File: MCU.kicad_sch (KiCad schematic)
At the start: 21 parts

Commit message: MCU updated to 48 pin
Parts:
- removed C58, C59, C71 (x2), C72, C73, C78 (x2): 0.1uF, Power_Analyzer:C_0603_1608Metric, symbol Power_Analyzer:0.1uF
- removed C74: 10uF, Power_Analyzer:C_0805_2012Metric, symbol Power_Analyzer:10uF
- removed C83: 2.2uF, Power_Analyzer:C_0603_1608Metric, symbol Power_Analyzer:2.2uF
- removed C?: 0.1uF, Capacitor_SMD:C_0603_1608Metric, symbol Major_Project:0.1uF
- removed C? (x2): 2.2uF, Capacitor_SMD:C_0603_1608Metric, symbol Major_Project:2.2uF
- removed R? (x2): 4.7K, Resistor_SMD:R_1206_3216Metric, symbol Major_Project:4.7K
- removed R? (x2): 10K, Resistor_SMD:R_1206_3216Metric, symbol Major_Project:10K
- removed U? (x4): F280037CSPZ, LQFP100_PZ_TEX, symbol Major_Project:F280037CSPZ
- added C1, C7: 2.2uF, Capacitor_SMD:C_0603_1608Metric, symbol Major_Project:2.2uF
- added C10, C2, C4, C5, C6, C8, C9: 0.1uF, Capacitor_SMD:C_0603_1608Metric, symbol Major_Project:0.1uF
- added C3: 10uF, Capacitor_SMD:C_0603_1608Metric, symbol Major_Project:10uF
- added J6: JTAG, Power_Analyzer:SAMTEC_FTSH-105-01-F-DV-K, symbol Power_Analyzer:FTSH-105-01-F-DV-K
- added R1, R4: 4.7K, Resistor_SMD:R_1206_3216Metric, symbol Major_Project:4.7K
- added R2, R3: 10K, Resistor_SMD:R_1206_3216Metric, symbol Major_Project:10K
- added U1: F280037CSPT, Power_Analyzer:PT0048A-MFG, symbol Major_Project:F280037CSPT
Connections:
- net +3.3V_2: now also C1.1, C10.1, C7.1, C8.1, C9.1, J6.01, R1.1, R2.1, R3.1, R4.1, U1.12 (VREFHI), U1.18 (VDDA), U1.24 (VDDIO), U1.35 (VDDIO), U1.46 (VDDIO)
- net GND_2: now also C1.2, C10.2, C2.2, C3.2, C4.2, C5.2, C6.2, C7.2, C8.2, C9.2, J6.03, J6.05, J6.09, U1.13 (VREFLO), U1.17 (VSSA), U1.22 (VSS), U1.37 (VSS), U1.44 (VSS)
- new net: C3.1, C4.1, C5.1, C6.1, U1.23 (VDD), U1.36 (VDD), U1.45 (VDD)
- new net: C2.1, R4.2, U1.3 (XRS_N)
- new net TCK: J6.04, U1.28 (TCK)
- new net TDI: J6.08, R2.2, U1.31 (GPIO35_TDI)
- new net TDO: J6.06, R3.2, U1.29 (GPIO37_TDO)
- new net TMS: J6.02, R1.2, U1.30 (TMS)
- no-connect marks 1 -> 2

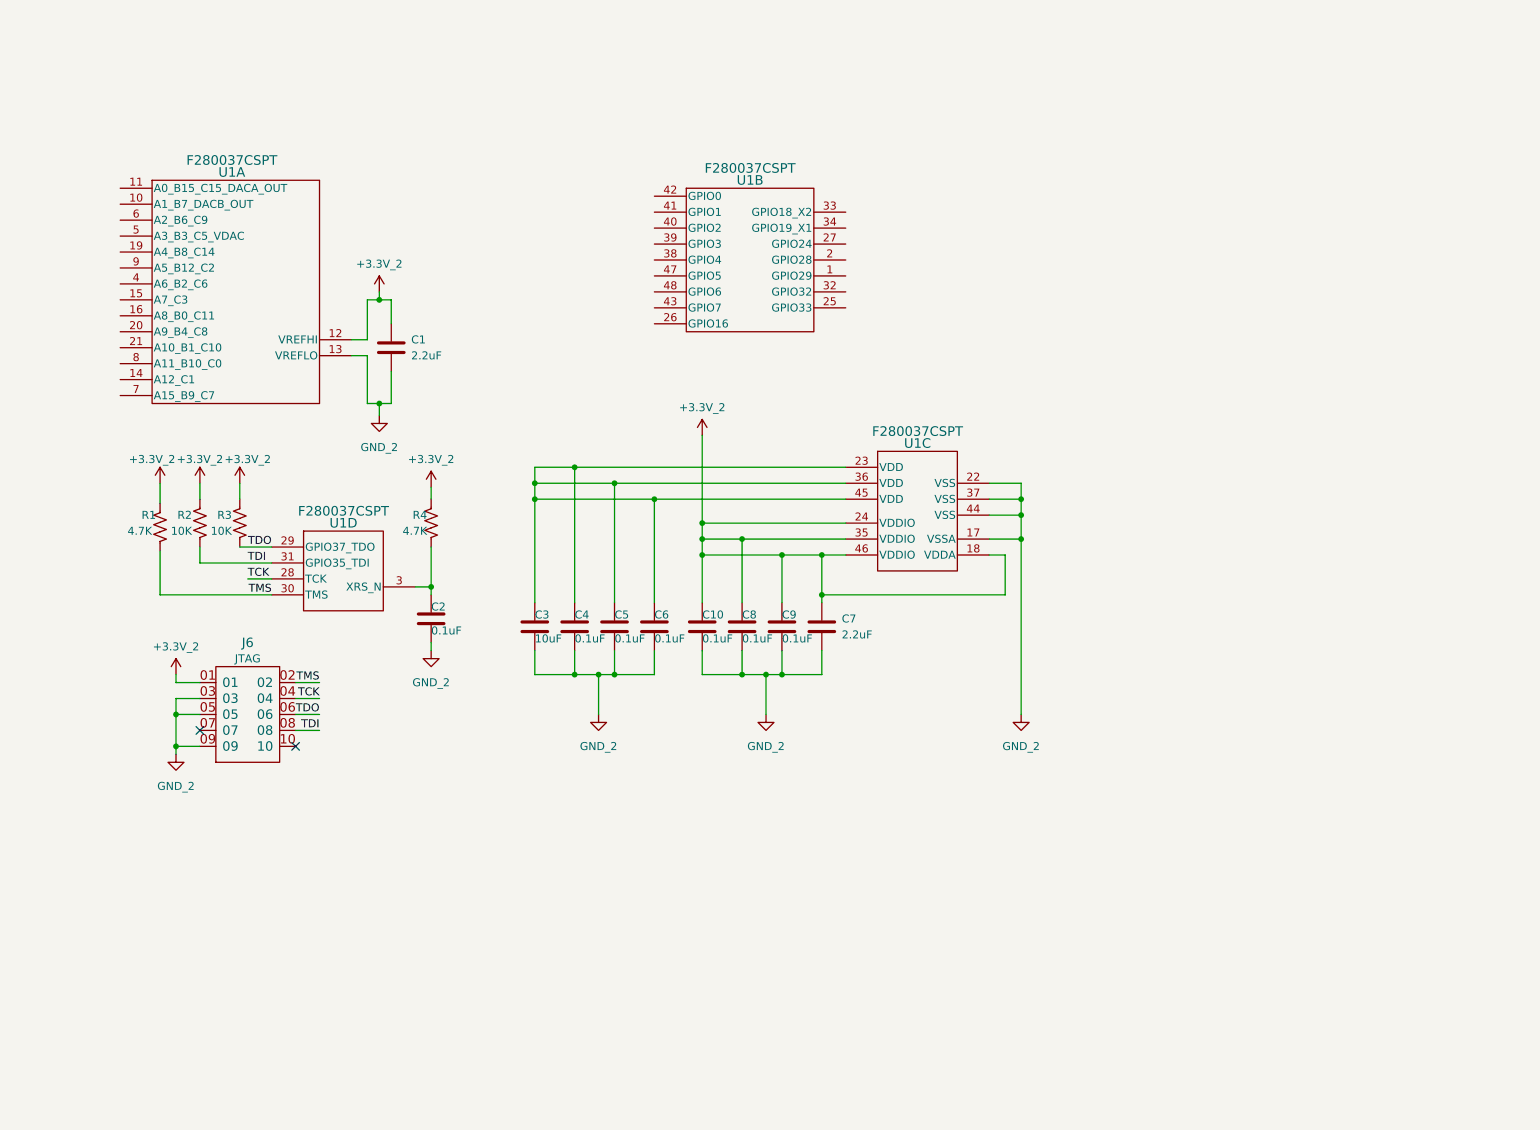
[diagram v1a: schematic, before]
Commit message: Current Sensing added
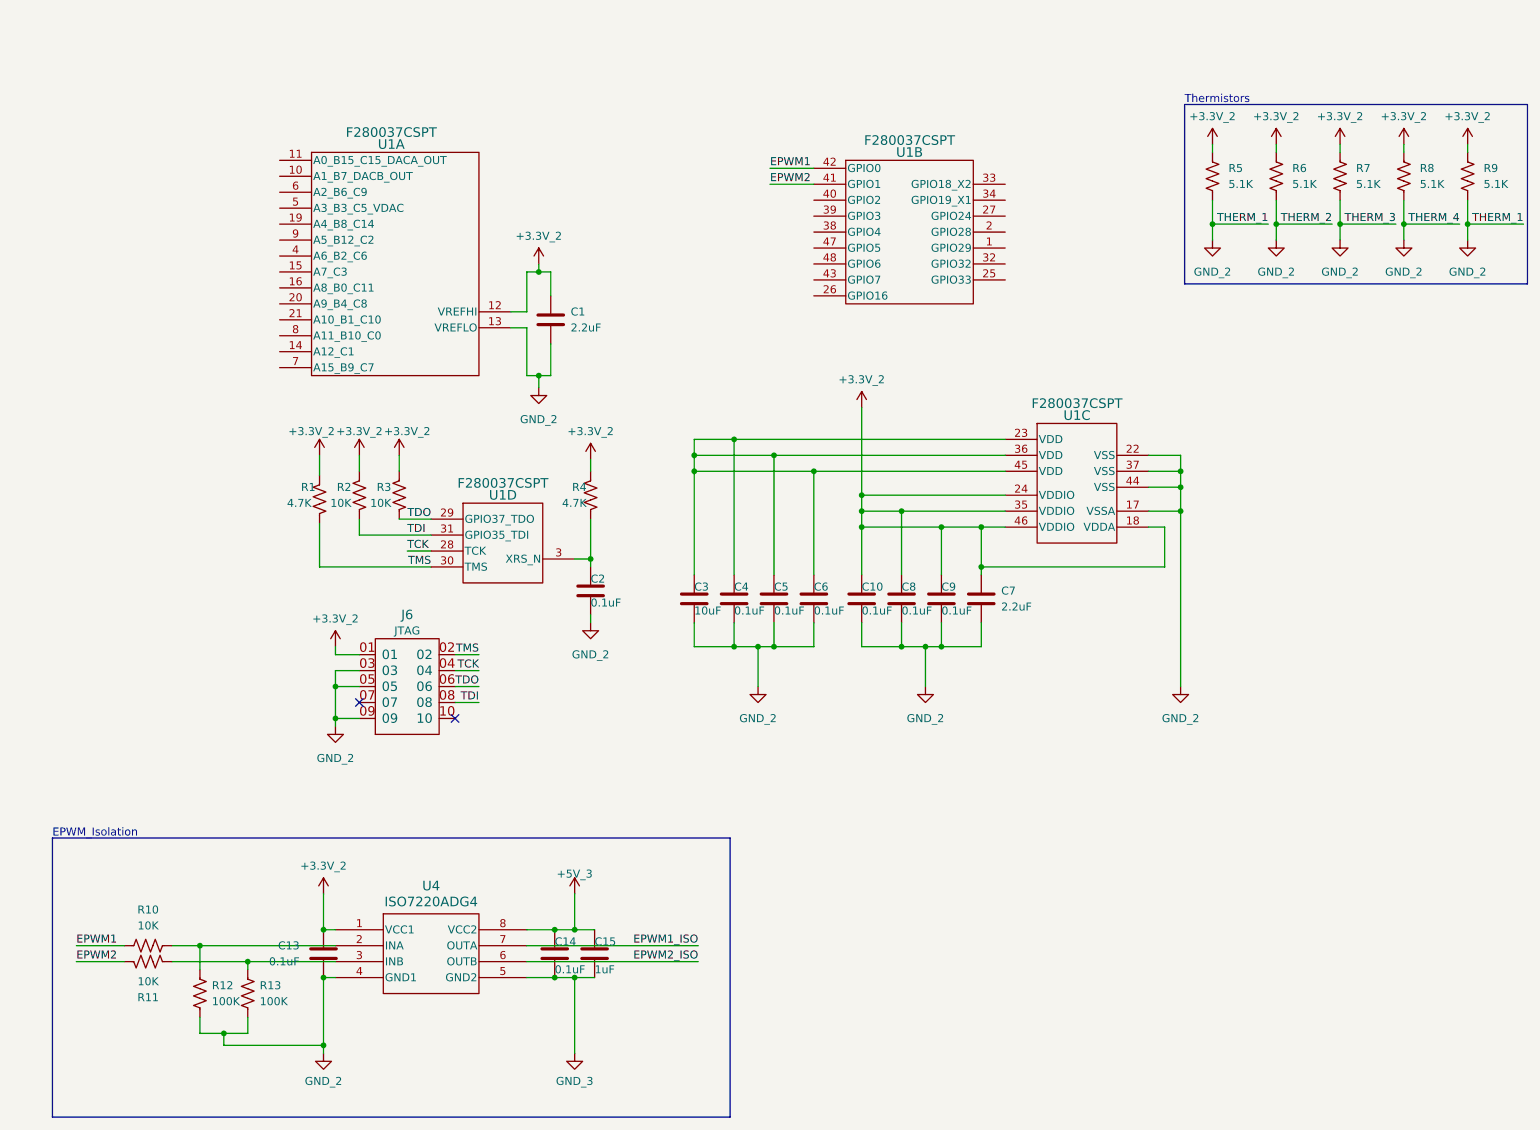
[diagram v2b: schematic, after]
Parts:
- added C13, C14: 0.1uF, Capacitor_SMD:C_0603_1608Metric, symbol Major_Project:0.1uF
- added C15: 1uF, Capacitor_SMD:C_0603_1608Metric, symbol Major_Project:1uF
- added R10, R11: 10K, Resistor_SMD:R_1206_3216Metric, symbol Major_Project:10K
- added R12, R13: 100K, Resistor_SMD:R_1206_3216Metric, symbol Major_Project:100K
- added R5, R6, R7, R8, R9: 5.1K, Resistor_SMD:R_1206_3216Metric, symbol Major_Project:5.1K
- added U4: ISO7220ADG4, D8, symbol Major_Project:ISO7220ADG4
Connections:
- net +3.3V_2: now also C13.1, R5.1, R6.1, R7.1, R8.1, R9.1, U4.1 (VCC1)
- net GND_2: now also C13.2, R12.2, R13.2, R5.2, R6.2, R7.2, R8.2, R9.2, U4.4 (GND1)
- net EPWM2: now reaches U1.41 (GPIO1)
- net EPWM2: now also R11.1
- net EPWM1: now reaches U1.42 (GPIO0)
- net EPWM1: now also R10.1
- new net: R10.2, R12.1, U4.2 (INA)
- new net: R11.2, R13.1, U4.3 (INB)
- new net +15V_1: C14.1, C15.1, U4.8 (VCC2)
- new net EPWM1_ISO: U4.7 (OUTA)
- new net EPWM2_ISO: U4.6 (OUTB)
- new net GND_3: C14.2, C15.2, U4.5 (GND2)
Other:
- note added: "EPWM_Isolation"
- note added: "Thermistors"
- moved on the sheet: C1, C10, C2, C3, C4, C5, C6, C7, C8, C9, J6, R1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
